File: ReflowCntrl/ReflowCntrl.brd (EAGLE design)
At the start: 86 x 54.6 mm, 13 parts, among them J1 DCJ0202, T1 2N2222, X1 1751248

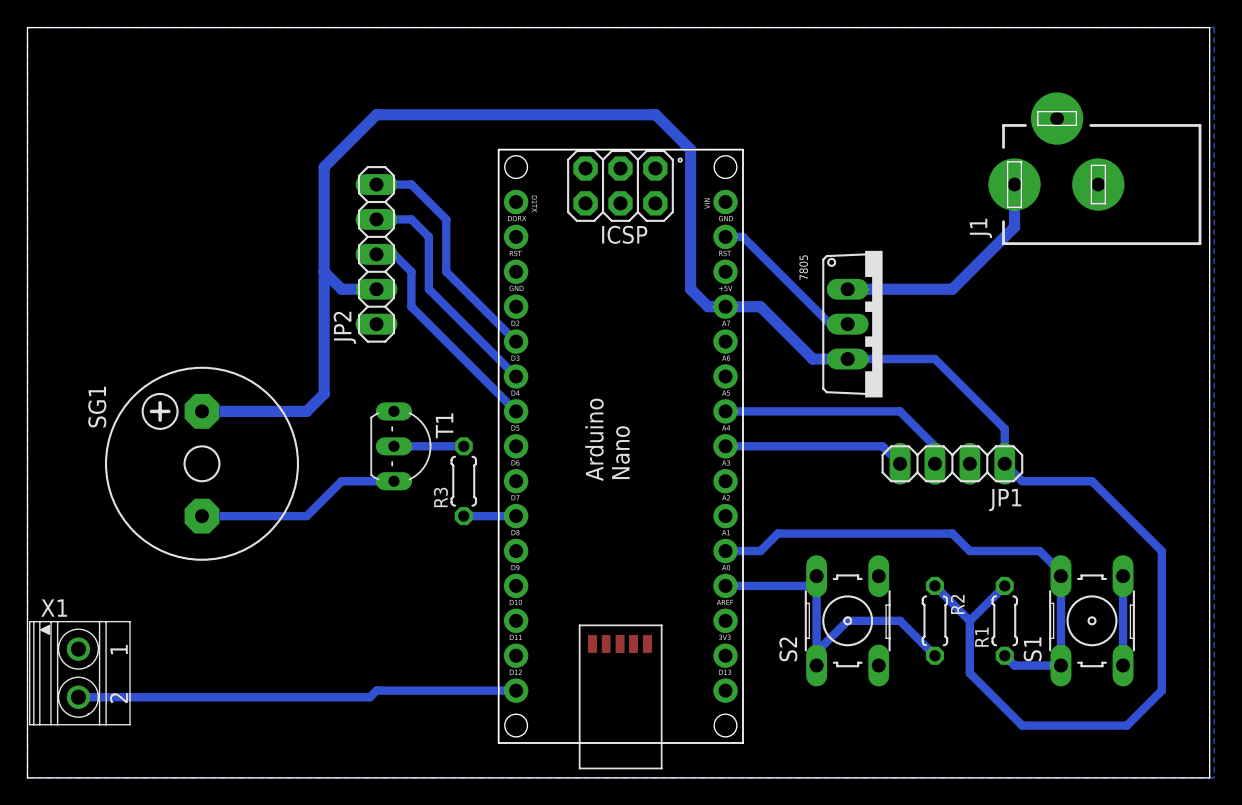
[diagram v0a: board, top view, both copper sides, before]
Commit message: Fix swapped VCC and GND pins on OLED. Resized board a bit.
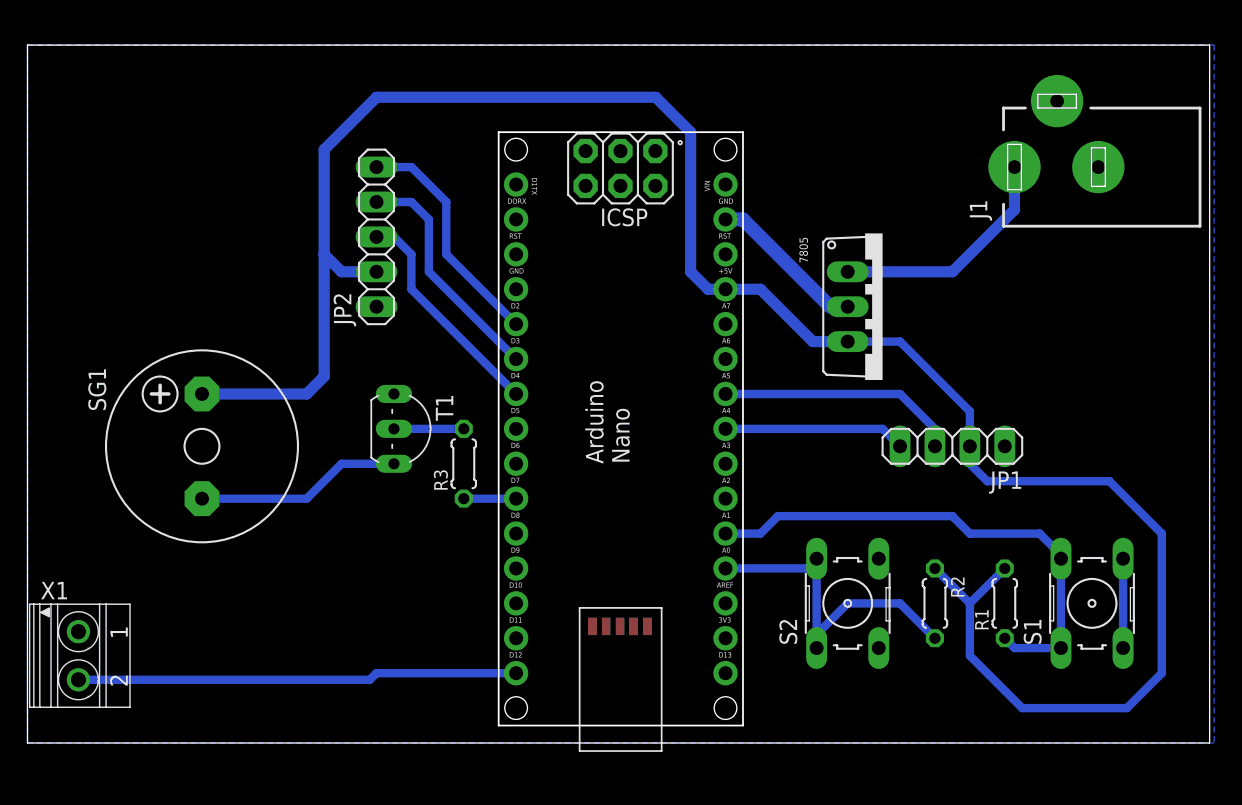
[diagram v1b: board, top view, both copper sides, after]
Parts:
- moved PCB1 1.27 mm to (52.1, 1.27)
- moved JP1 1.27 mm to (67.3, 21.6)
- moved R1 1.27 mm to (71.1, 10.2)
- moved R2 1.27 mm to (66.0, 10.2)
- moved R3 1.27 mm to (31.8, 20.3)
- moved S1 1.27 mm to (77.5, 10.2)
- moved S2 1.27 mm to (59.7, 10.2)
- moved SG1 1.27 mm to (12.7, 21.6)
- moved T1 1.27 mm to (27.9, 22.9)
- moved U$1 1.27 mm to (62.2, 31.8)
- moved X1 1.27 mm to (3.81, 6.35)
- moved J1 1.27 mm to (74.9, 41.9)
- moved JP2 1.27 mm to (25.4, 36.8)
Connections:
- net GND: now also JP1.1; no longer JP1.2
- net VCC: now also JP1.2; no longer JP1.1
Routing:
- net VCC: track 151.1 -> 151.9 mm
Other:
- board size 86 x 54.6 mm -> 86 x 50.8 mm
